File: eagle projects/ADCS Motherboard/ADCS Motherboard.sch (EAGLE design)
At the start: 144 parts, among them J1 HDR_10_EZFET_DEBUGGER, J11 CNC_3221-10-0300-00, J5 CNC_3221-10-0300-00, J7 TE-1734829-3, Q1 BSR802NL6327HTSA1, U1 MSP430F5529IPN, U10 TSV991AILT, U2 TSV991AILT, U3 ADS7841E_2K5, U4 TSV991AILT, U5 DMC4050SSDQ-13, U6 BNO055, U7 HMC1053, U9 BMX160, Y1 32.768kHz, Y2 CSTCR4M00G15L99, Y3 32.768kHz

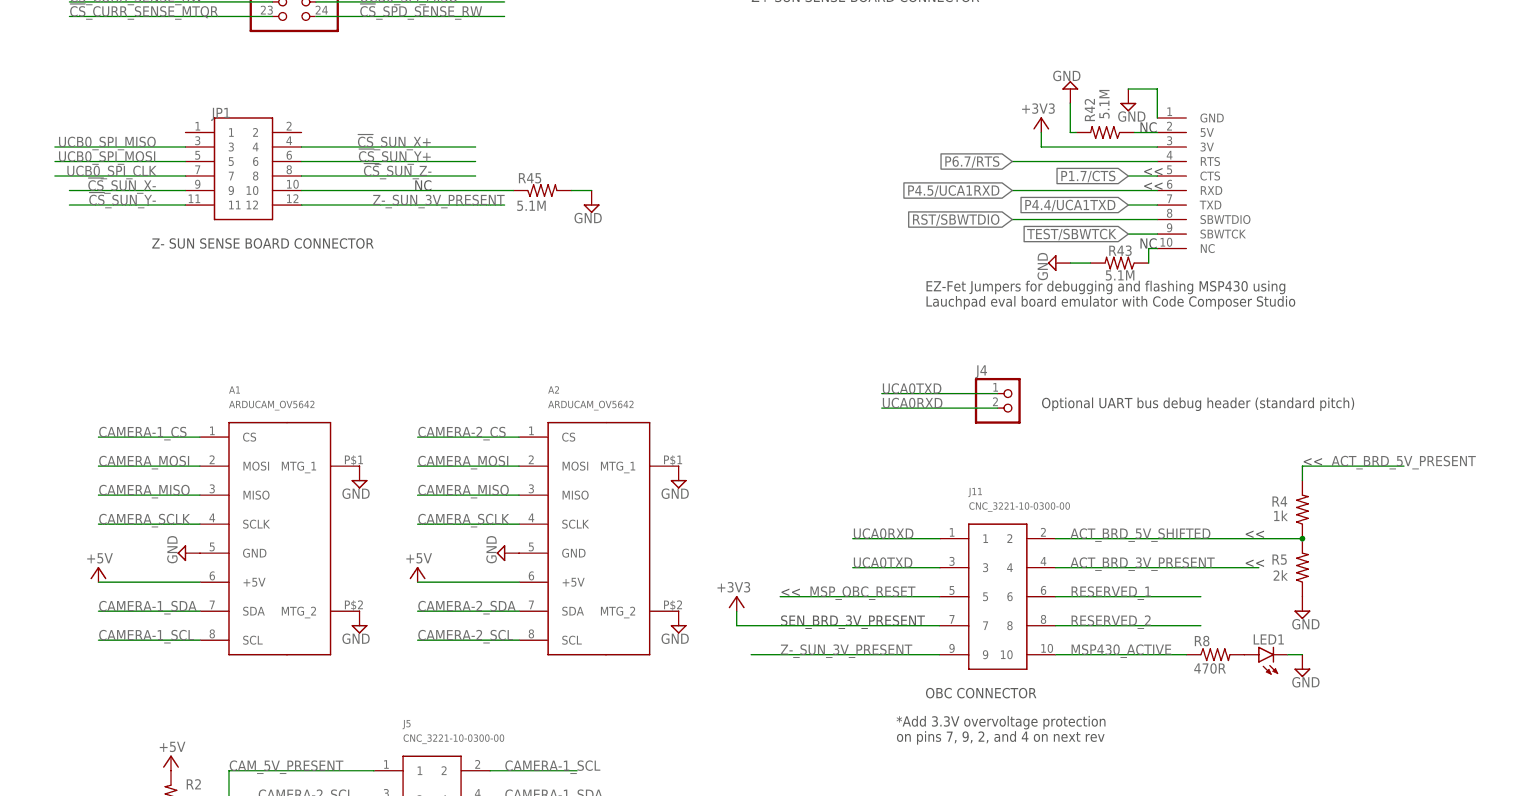
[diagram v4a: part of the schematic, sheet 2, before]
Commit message: Changed out OBC connector on motherboard
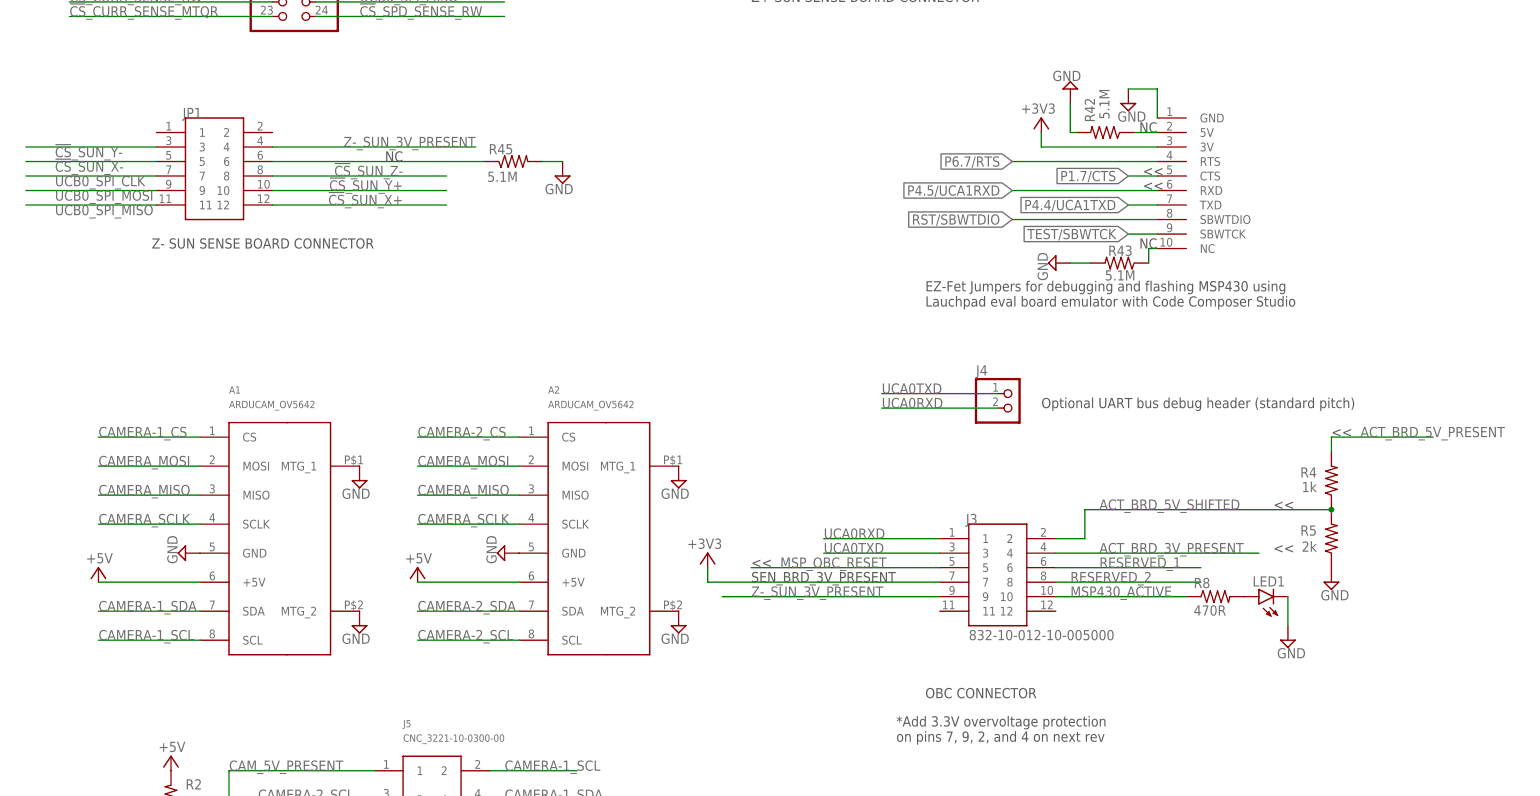
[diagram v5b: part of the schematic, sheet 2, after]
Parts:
- removed J11: CNC_3221-10-0300-00, my_library:CNC_3221-10-0300-00
- added J3: 832-10-012-10-005000, 832-10-012-10-005000:832-10-012-10-005000
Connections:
- net !CS!_SUN_X+: now also JP1.12; no longer JP1.4
- net !CS!_SUN_X-: now also JP1.5; no longer JP1.9
- net !CS!_SUN_Y+: now also JP1.10; no longer JP1.6
- net !CS!_SUN_Y-: now also JP1.3; no longer JP1.11
- net +3V3: now also J3.7; no longer J11.7
- net ACT_BRD_3V_PRESENT: now also J3.4; no longer J11.4
- net ACT_BRD_5V_SHIFTED: now also J3.2; no longer J11.2
- net MSP430_ACTIVE: now also J3.10; no longer J11.10
- net MSP_OBC_RESET: now also J3.5; no longer J11.5
- net N$58: now also JP1.6; no longer JP1.10
- net RESERVED_1: now also J3.6; no longer J11.6
- net RESERVED_2: now also J3.8; no longer J11.8
- net UCA0RXD: now also J3.1; no longer J11.1
- net UCA0TXD: now also J3.3; no longer J11.3
- net UCB0_SPI_MISO: now also JP1.11; no longer JP1.3
- net UCB0_SPI_MOSI: now also JP1.9; no longer JP1.5
- net Z-_SUN_3V_PRESENT: now also J3.9, JP1.4; no longer J11.9, JP1.12
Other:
- moved on the sheet: JP1, LED1, R4, R45, R5, R8
